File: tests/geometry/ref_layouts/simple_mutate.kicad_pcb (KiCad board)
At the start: 2 copper layers, 0 parts

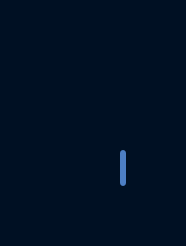
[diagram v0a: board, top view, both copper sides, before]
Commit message: Mutation tests (loading a source board, modifying, saving, compare to reference)
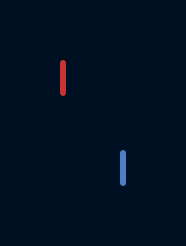
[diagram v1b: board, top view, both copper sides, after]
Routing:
- net (no net): track 1.00 -> 2.00 mm
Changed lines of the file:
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@@
   )
   (net 0 "")
+  (segment (start -1 -1) (end -1 -2) (width 0.2) (layer "F.Cu") (net 0))
   (segment (start 1 1) (end 1 2) (width 0.2) (layer "B.Cu") (net 0))
 )
